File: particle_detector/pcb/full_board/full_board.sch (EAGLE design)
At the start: 43 parts, among them IC1 LT1807R, IC2 TLV3501, IC3 LT3461, IC4 TEENSY 3.2, IC5 SENSL-SIPM

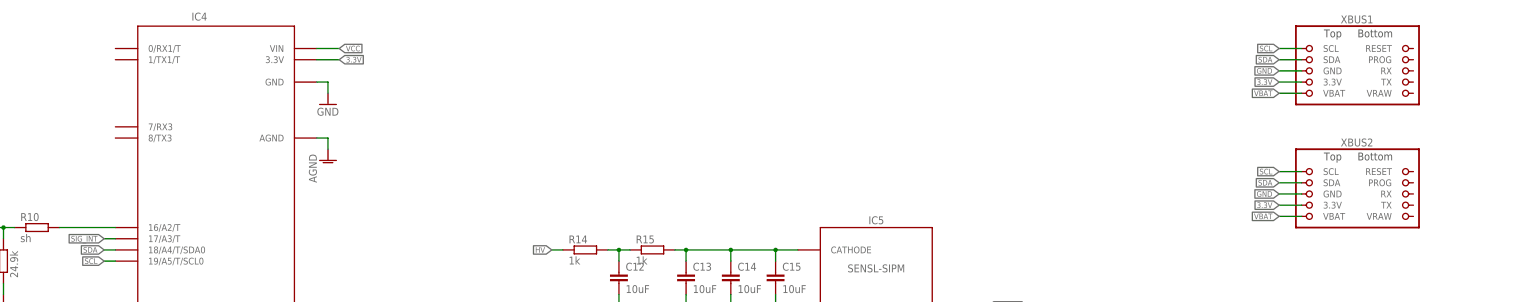
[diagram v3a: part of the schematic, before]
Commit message: layout TX/RX and change power to 5V; send to PCBWay 2019.05.29
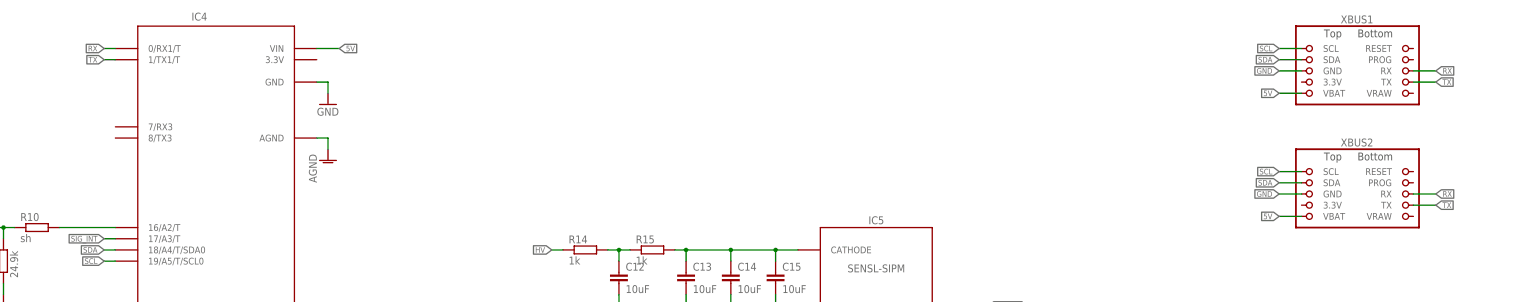
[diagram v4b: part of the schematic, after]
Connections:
- removed net VBAT: XBUS1.VBAT, XBUS2.VBAT
- removed net VCC: IC4.VIN
- new net 5V: IC4.VIN, XBUS1.VBAT, XBUS2.VBAT
- new net RX: IC4.0/RX1/T, XBUS1.RX, XBUS2.RX
- new net TX: IC4.1/TX1/T, XBUS1.TX, XBUS2.TX
- net 3.3V: no longer IC4.3.3V, XBUS1.3.3V, XBUS2.3.3V
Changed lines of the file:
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@@
 <wire x1="276.86" y1="162.56" x2="276.86" y2="220.98" width="0.1524" layer="98" style="shortdash"/>
 <wire x1="276.86" y1="220.98" x2="152.4" y2="220.98" width="0.1524" layer="98" style="shortdash"/>
-<wire x1="312.42" y1="261.62" x2="370.84" y2="261.62" width="0.1524" layer="98" style="shortdash"/>
-<wire x1="370.84" y1="261.62" x2="370.84" y2="200.66" width="0.1524" layer="98" style="shortdash"/>
-<wire x1="370.84" y1="200.66" x2="312.42" y2="200.66" width="0.1524" layer="98" style="shortdash"/>
+<wire x1="312.42" y1="261.62" x2="388.62" y2="261.62" width="0.1524" layer="98" style="shortdash"/>
+<wire x1="388.62" y1="261.62" x2="388.62" y2="200.66" width="0.1524" layer="98" style="shortdash"/>
+<wire x1="388.62" y1="200.66" x2="312.42" y2="200.66" width="0.1524" layer="98" style="shortdash"/>
 <wire x1="312.42" y1="200.66" x2="312.42" y2="261.62" width="0.1524" layer="98" style="shortdash"/>
 <text x="210.82" y="215.9" size="2.54" layer="98" align="bottom-center">Detector</text>
@@
 </segment>
 </net>
-<net name="VCC" class="0">
-<segment>
-<pinref part="IC4" gate="G$1" pin="VIN"/>
-<wire x1="109.22" y1="246.38" x2="114.3" y2="246.38" width="0.1524" layer="91"/>
-<label x="114.3" y="246.38" size="1.27" layer="95" xref="yes"/>
-</segment>
-</net>
 <net name="SDA" class="0">
 <segment>
@@
 </net>
 <net name="3.3V" class="0">
-<segment>
-<pinref part="XBUS1" gate="G$1" pin="3.3V"/>
-<wire x1="332.74" y1="238.76" x2="327.66" y2="238.76" width="0.1524" layer="91"/>
-<label x="327.66" y="238.76" size="1.27" layer="95" rot="R180" xref="yes"/>
-</segment>
-<segment>
-<pinref part="IC4" gate="G$1" pin="3.3V"/>
-<wire x1="109.22" y1="243.84" x2="114.3" y2="243.84" width="0.1524" layer="91"/>
-<label x="114.3" y="243.84" size="1.27" layer="95" xref="yes"/>
-</segment>
 <segment>
 <pinref part="IC1" gate="P" pin="V+"/>
@@
 <pinref part="L1" gate="G$1" pin="1"/>
 </segment>
-<segment>
-<pinref part="XBUS2" gate="G$1" pin="3.3V"/>
-<wire x1="332.74" y1="210.82" x2="327.66" y2="210.82" width="0.1524" layer="91"/>
-<label x="327.66" y="210.82" size="1.27" layer="95" rot="R180" xref="yes"/>
-</segment>
-</net>
-<net name="VBAT" class="0">
-<segment>
-<pinref part="XBUS1" gate="G$1" pin="VBAT"/>
-<wire x1="332.74" y1="236.22" x2="327.66" y2="236.22" width="0.1524" layer="91"/>
-<label x="327.66" y="236.22" size="1.27" layer="95" rot="R180" xref="yes"/>
-</segment>
-<segment>
-<pinref part="XBUS2" gate="G$1" pin="VBAT"/>
-<wire x1="332.74" y1="208.28" x2="327.66" y2="208.28" width="0.1524" layer="91"/>
-<label x="327.66" y="208.28" size="1.27" layer="95" rot="R180" xref="yes"/>
-</segment>
 </net>
 <net name="AGND" class="0">
@@
 </segment>
 </net>
+<net name="RX" class="0">
+<segment>
+<pinref part="IC4" gate="G$1" pin="0/RX1/T"/>
+<wire x1="63.5" y1="246.38" x2="60.96" y2="246.38" width="0.1524" layer="91"/>
+<label x="60.96" y="246.38" size="1.27" layer="95" rot="R180" xref="yes"/>
+</segment>
+<segment>
+<pinref part="XBUS1" gate="G$1" pin="RX"/>
+<wire x1="358.14" y1="241.3" x2="363.22" y2="241.3" width="0.1524" layer="91"/>
+<label x="363.22" y="241.3" size="1.27" layer="95" xref="yes"/>
+</segment>
+<segment>
+<pinref part="XBUS2" gate="G$1" pin="RX"/>
+<wire x1="358.14" y1="213.36" x2="363.22" y2="213.36" width="0.1524" layer="91"/>
+<label x="363.22" y="213.36" size="1.27" layer="95" xref="yes"/>
+</segment>
+</net>
+<net name="TX" class="0">
+<segment>
+<pinref part="IC4" gate="G$1" pin="1/TX1/T"/>
+<wire x1="63.5" y1="243.84" x2="60.96" y2="243.84" width="0.1524" layer="91"/>
+<label x="60.96" y="243.84" size="1.27" layer="95" rot="R180" xref="yes"/>
+</segment>
+<segment>
+<pinref part="XBUS1" gate="G$1" pin="TX"/>
+<wire x1="358.14" y1="238.76" x2="363.22" y2="238.76" width="0.1524" layer="91"/>
+<label x="363.22" y="238.76" size="1.27" layer="95" xref="yes"/>
+</segment>
+<segment>
+<pinref part="XBUS2" gate="G$1" pin="TX"/>
+<wire x1="358.14" y1="210.82" x2="363.22" y2="210.82" width="0.1524" layer="91"/>
+<label x="363.22" y="210.82" size="1.27" layer="95" xref="yes"/>
+</segment>
+</net>
+<net name="5V" class="0">
+<segment>
+<pinref part="XBUS1" gate="G$1" pin="VBAT"/>
+<wire x1="332.74" y1="236.22" x2="327.66" y2="236.22" width="0.1524" layer="91"/>
+<label x="327.66" y="236.22" size="1.27" layer="95" rot="R180" xref="yes"/>
+</segment>
+<segment>
+<pinref part="XBUS2" gate="G$1" pin="VBAT"/>
+<wire x1="332.74" y1="208.28" x2="327.66" y2="208.28" width="0.1524" layer="91"/>
+<label x="327.66" y="208.28" size="1.27" layer="95" rot="R180" xref="yes"/>
+</segment>
+<segment>
+<pinref part="IC4" gate="G$1" pin="VIN"/>
+<wire x1="109.22" y1="246.38" x2="114.3" y2="246.38" width="0.1524" layer="91"/>
+<label x="114.3" y="246.38" size="1.27" layer="95" xref="yes"/>
+</segment>
+</net>

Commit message: final routing for elecrow production, sent 2020.02.21
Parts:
- removed C10: 0.1uF, rcl:C-EUC0805
- removed C11: 2.2uF, rcl:C-EUC0805
- removed IC2: TLV3501, AU_Thinsat_Comparators:TLV3501
- removed R11, R13: 47, resistor:R-EU_M0805
- removed R12: 470, resistor:R-EU_M0805
- removed TOUCH: (no value), pinhead:PINHD-1X4
- added AMP, PEAK, RAW: (no value), pinhead:PINHD-1X1
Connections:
- removed net N$5: IC2.IN-, R11.2, R12.2
- removed net SIG_INT: IC2.OUT, IC4.17/A3/T, R13.2, TOUCH.4
- net 3.3V: no longer C10.1, C11.1, IC2.V+, R12.1
- net AGND: no longer IC2.SHDN, IC2.V-, R11.1
- net GND: no longer C10.2, C11.2, R13.1
- net SIG_AMP: now also AMP.1; no longer IC2.IN+, TOUCH.2
- net SIG_PEAK: now also PEAK.1; no longer TOUCH.3
- net SIG_RAW: now also RAW.1; no longer TOUCH.1
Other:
- note removed: "Interrupt Generation"

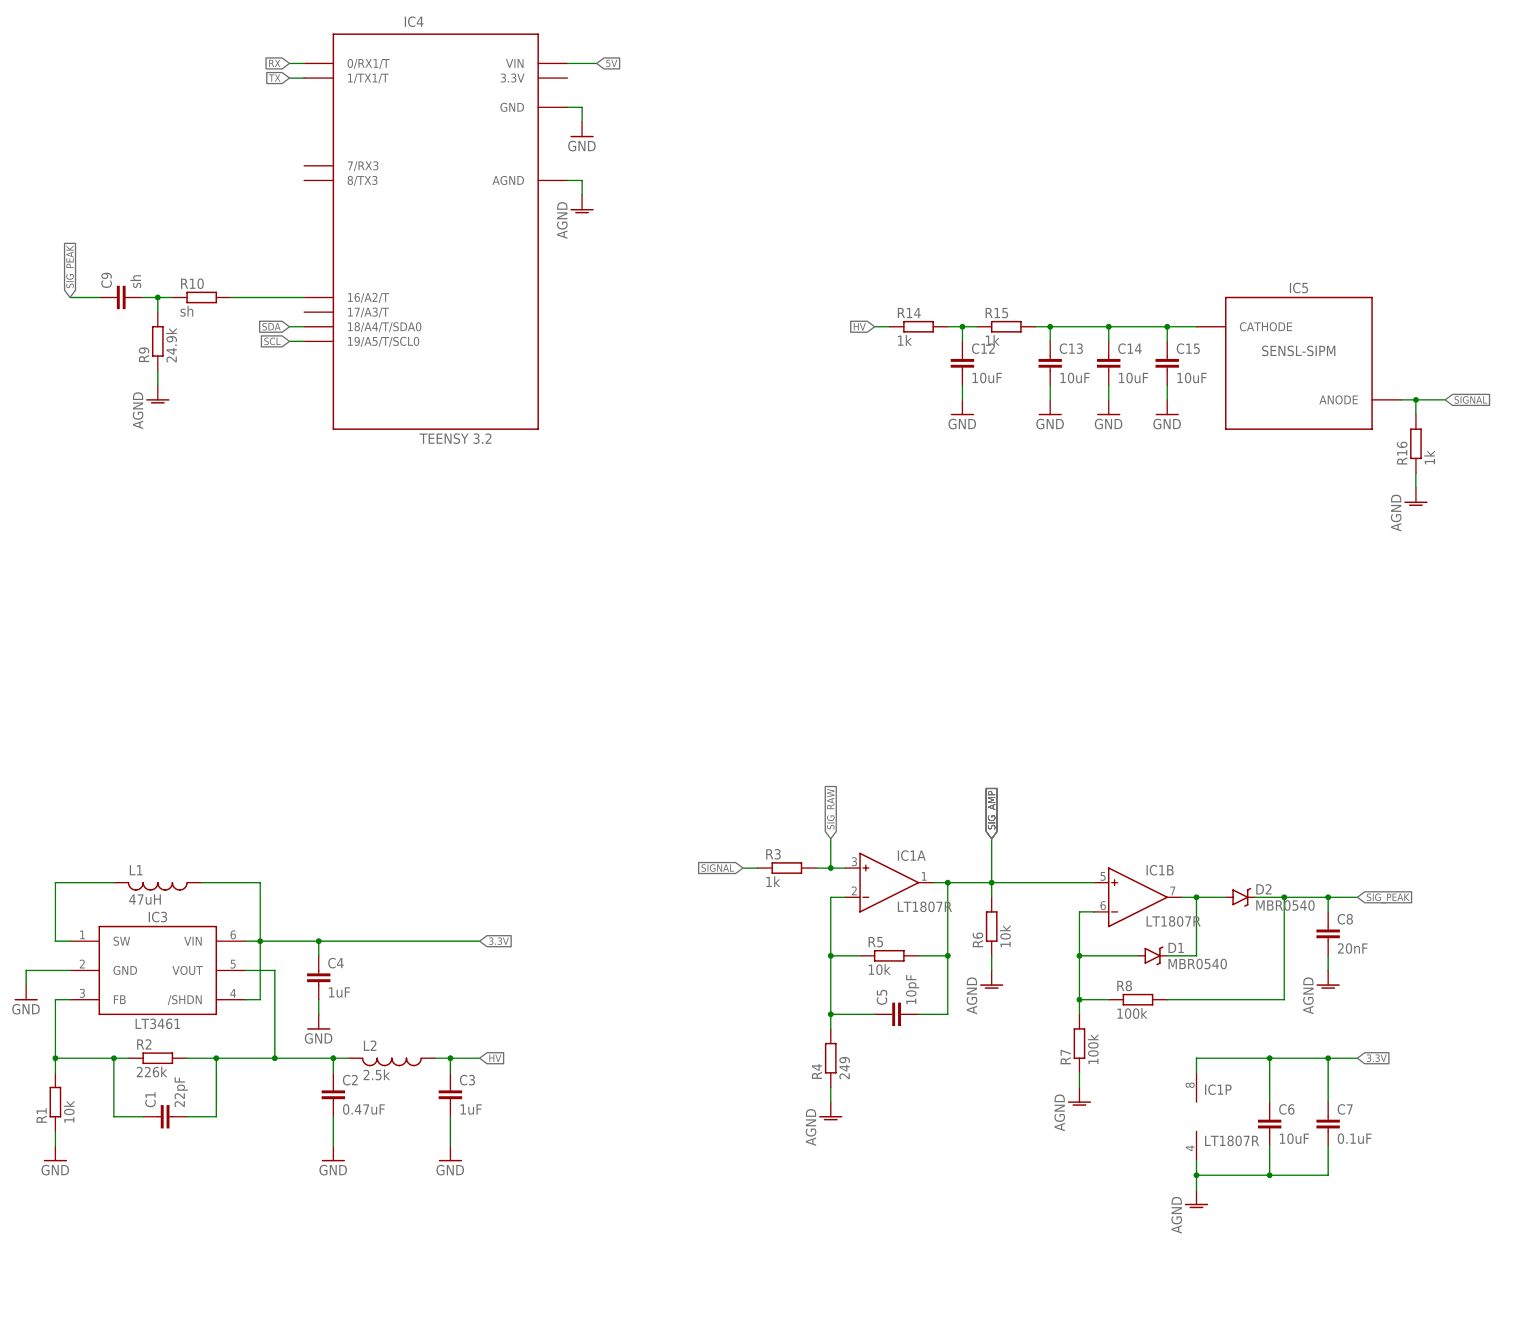
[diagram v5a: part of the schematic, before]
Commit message: Swap the Teensy3.2 for the ATTiny and update nets.
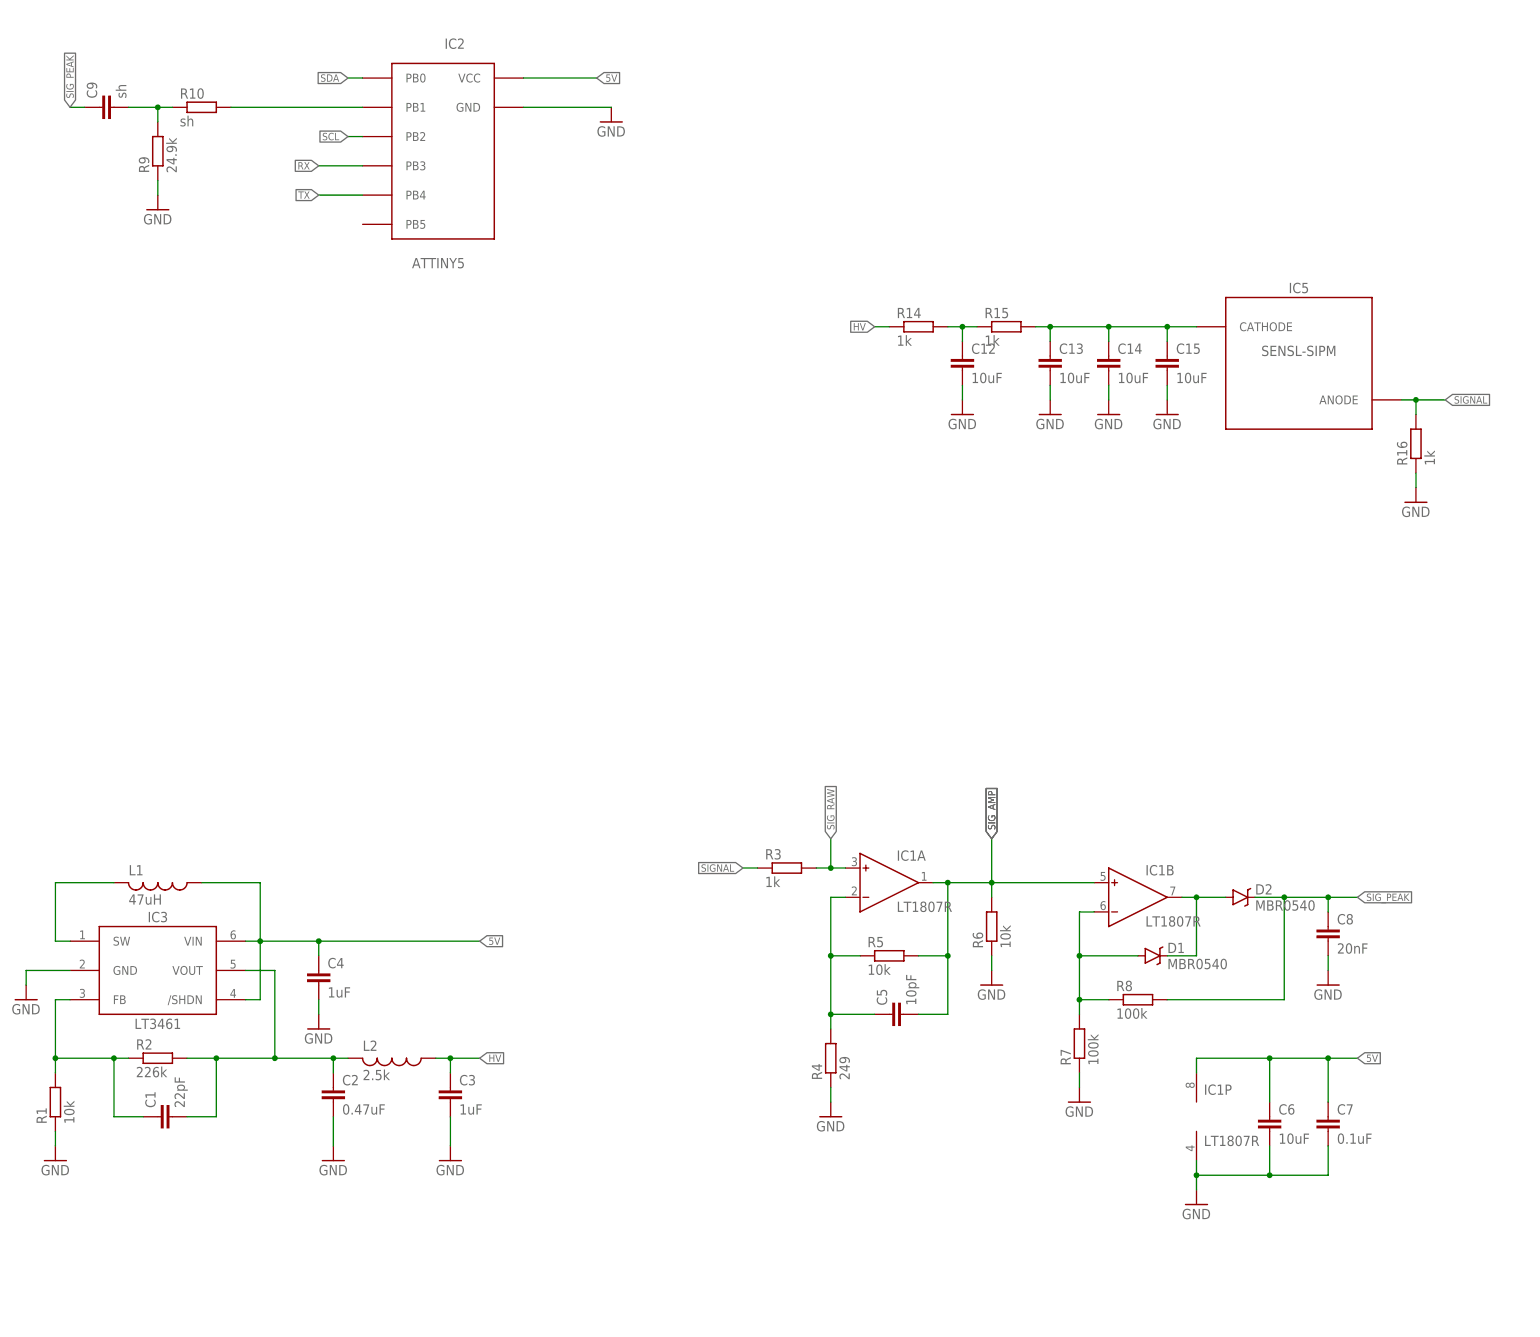
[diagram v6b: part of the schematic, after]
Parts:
- removed IC4: TEENSY 3.2, personal:TEENSY_3.2_THINSAT
- added IC2: ATTINY5, personal:ATTINY5
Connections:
- removed net 3.3V: C4.1, C6.1, C7.1, IC1P.V+, IC3./SHDN, IC3.VIN, L1.1
- removed net AGND: C6.2, C7.2, C8.2, IC1P.V-, IC4.AGND, R16.1, R4.1, R6.1, R7.1, R9.1
- net 5V: now also C4.1, C6.1, C7.1, IC1P.V+, IC2.VCC, IC3./SHDN, IC3.VIN, L1.1; no longer IC4.VIN
- net GND: now also C6.2, C7.2, C8.2, IC1P.V-, IC2.GND, R16.1, R4.1, R6.1, R7.1, R9.1; no longer IC4.GND
- net N$10: now also IC2.PB1; no longer IC4.16/A2/T
- net RX: now also IC2.PB3; no longer IC4.0/RX1/T
- net SCL: now also IC2.PB2; no longer IC4.19/A5/T/SCL0
- net SDA: now also IC2.PB0; no longer IC4.18/A4/T/SDA0
- net TX: now also IC2.PB4; no longer IC4.1/TX1/T
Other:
- moved on the sheet: C9, R10, R9

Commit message: Change ATTiny pads to save space
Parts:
- IC1: device personal:LT1807R -> Personal:LT1807R
- IC2: device personal:ATTINY5 -> Personal:ATTINY5
- IC3: device personal:LT3461 -> Personal:LT3461
- IC5: device personal:SENSL-SIPM -> Personal:SENSL-SIPM
- XBUS1, XBUS2: device personal:XINABOX-XBUS -> Personal:XINABOX-XBUS
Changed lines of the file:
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@@
 <part name="R9" library="rcl" deviceset="R-EU_" device="M0805" value="24.9k"/>
 <part name="R10" library="rcl" deviceset="R-EU_" device="M0805" value="sh"/>
-<part name="IC3" library="personal" deviceset="LT3461" device=""/>
-<part name="IC1" library="personal" deviceset="LT1807" device="R" package3d_urn="urn:adsk.eagle:package:3906/1"/>
+<part name="IC3" library="Personal" deviceset="LT3461" device=""/>
+<part name="IC1" library="Personal" deviceset="LT1807" device="R" package3d_urn="urn:adsk.eagle:package:3906/1"/>
 <part name="C1" library="rcl" deviceset="C-EU" device="C0805K" value="22pF"/>
 <part name="C2" library="rcl" deviceset="C-EU" device="C0805K" value="0.47uF"/>
@@
 <part name="D2" library="SparkFun-DiscreteSemi" deviceset="DIODE-SCHOTTKY" device="-B340A" value="MBR0540"/>
 <part name="GND23" library="supply1" deviceset="GND" device=""/>
-<part name="XBUS1" library="personal" deviceset="XINABOX-XBUS" device=""/>
-<part name="L1" library="rcl" library_urn="urn:adsk.eagle:library:334" deviceset="L-US" device="L3225M" package3d_urn="urn:adsk.eagle:package:23477/1" value="47uH"/>
-<part name="IC5" library="personal" deviceset="SENSL-SIPM" device=""/>
+<part name="XBUS1" library="Personal" deviceset="XINABOX-XBUS" device=""/>
+<part name="L1" library="rcl" library_urn="urn:adsk.eagle:library:334" deviceset="L-US" device="L3225M" package3d_urn="urn:adsk.eagle:package:23477/2" value="47uH"/>
+<part name="IC5" library="Personal" deviceset="SENSL-SIPM" device=""/>
 <part name="C12" library="rcl" deviceset="C-EU" device="C0805K" value="10uF"/>
 <part name="C13" library="rcl" deviceset="C-EU" device="C0805K" value="10uF"/>
@@
 <part name="GND14" library="supply1" deviceset="GND" device=""/>
 <part name="GND19" library="supply1" deviceset="GND" device=""/>
-<part name="XBUS2" library="personal" deviceset="XINABOX-XBUS" device=""/>
+<part name="XBUS2" library="Personal" deviceset="XINABOX-XBUS" device=""/>
 <part name="RAW" library="pinhead" library_urn="urn:adsk.eagle:library:325" deviceset="PINHD-1X1" device="" package3d_urn="urn:adsk.eagle:package:22485/2"/>
 <part name="AMP" library="pinhead" library_urn="urn:adsk.eagle:library:325" deviceset="PINHD-1X1" device="" package3d_urn="urn:adsk.eagle:package:22485/2"/>
 <part name="PEAK" library="pinhead" library_urn="urn:adsk.eagle:library:325" deviceset="PINHD-1X1" device="" package3d_urn="urn:adsk.eagle:package:22485/2"/>
-<part name="IC2" library="personal" deviceset="ATTINY*5" device=""/>
+<part name="IC2" library="Personal" deviceset="ATTINY*5" device=""/>
 <part name="GND1" library="supply1" library_urn="urn:adsk.eagle:library:371" deviceset="GND" device=""/>
 <part name="GND2" library="supply1" library_urn="urn:adsk.eagle:library:371" deviceset="GND" device=""/>
